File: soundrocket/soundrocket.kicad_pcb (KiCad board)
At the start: 4 copper layers, 85.3 x 45.7 mm, 17 parts, among them J1 XLR3 MALE (OUT), SW1 SW_Push, SW2 RotaryEncoder_Switch, T1 PE-65612NL, U1 Teensy4.0, U2 DIT4192IPW

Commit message: Prototype Revision 2
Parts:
- renumbered R1 to PUR1, R2 to PUR2, R5 to PUR5
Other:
- board text added: "Designed by Daniel A"
- board text added: "sr-proto-rev2"
- board text removed: "Designed by Daniel A."
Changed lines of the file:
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@@
 		(tags "rotary encoder")
 		(property "Reference" "SW2"
-			(at 3 -4.75 0)
+			(at 2.995 -4.866 0)
 			(layer "F.SilkS")
 			(effects
@@
 		(tags "test point THT pad")
 		(property "Reference" "GND"
-			(at 0 -1.648 0)
+			(at 0 -2.032 0)
 			(layer "F.SilkS")
 			(effects
@@
 		)
 		(property "Value" "GND"
-			(at 0 1.75 0)
+			(at 0 2.032 0)
 			(layer "F.Fab")
 			(effects
@@
 		)
 		(fp_text user "GND"
-			(at 0 -1.65 0)
+			(at 0 -2.032 0)
 			(layer "F.Fab")
 			(effects
@@
 		(at 122.428 51.308 -90)
 		(tags "CF14JT10K0 ")
-		(property "Reference" "R5"
-			(at 5.715 0 270)
+		(property "Reference" "PUR5"
+			(at 14.478 0 270)
 			(unlocked yes)
 			(layer "F.SilkS")
@@
 		(tags "test point THT pad")
 		(property "Reference" "5V"
-			(at 0 -1.648 0)
+			(at 0 -2.032 0)
 			(layer "F.SilkS")
 			(effects
@@
 		)
 		(property "Value" "5V"
-			(at 0 1.75 0)
+			(at 0 2.032 0)
 			(layer "F.Fab")
 			(effects
@@
 		)
 		(fp_text user "5V"
-			(at 0 -1.65 0)
+			(at 0 -2.032 0)
 			(layer "F.Fab")
 			(effects
@@
 		(at 165.608 67.31)
 		(tags "CF14JT10K0 ")
-		(property "Reference" "R2"
-			(at 13.462 0 0)
+		(property "Reference" "PUR2"
+			(at 14.478 0 0)
 			(unlocked yes)
 			(layer "F.SilkS")
@@
 		(tags "tact sw push 12mm")
 		(property "Reference" "SW1"
-			(at 5.83 -5.41 90)
+			(at 6.25 9.572 270)
 			(layer "F.SilkS")
 			(effects
@@
 		(at 165.608 71.374)
 		(tags "CF14JT10K0 ")
-		(property "Reference" "R1"
-			(at 13.462 0 0)
+		(property "Reference" "PUR1"
+			(at 14.478 0 0)
 			(unlocked yes)
 			(layer "F.SilkS")
@@
 		)
 	)
-	(gr_text "Designed by Daniel A."
-		(at 130.81 30.226 0)
+	(gr_text "sr-proto-rev2"
+		(at 195.326 71.628 0)
+		(layer "F.SilkS")
+		(effects
+			(font
+				(size 0.8 0.8)
+				(thickness 0.16)
+				(bold yes)
+			)
+			(justify left bottom)
+		)
+	)
+	(gr_text "Designed by Daniel A"
+		(at 191.008 73.152 0)
 		(layer "F.SilkS")
 		(effects
 			(font
-				(size 1.5 1.5)
-				(thickness 0.3)
+				(size 0.8 0.8)
+				(thickness 0.16)
 				(bold yes)
 			)

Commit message: Shrink
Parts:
- removed 5V: 5V, TestPoint:TestPoint_THTPad_D1.5mm_Drill0.7mm
- removed C2, C3, C4: C_Small, KiCad Models:CAPRR254W54L381T254H466
- removed GND: GND, TestPoint:TestPoint_THTPad_D1.5mm_Drill0.7mm
- removed J1: XLR3 MALE (OUT), Connector_Audio:Jack_XLR_Neutrik_NC3MAAV_Vertical
- removed PUR1, PUR2, R3, R4: R_Small (10k), KiCad Models:STA_CF14_STP
- removed PUR5: R_Small, KiCad Models:STA_CF14_STP
- removed SW2: RotaryEncoder_Switch, Rotary_Encoder:RotaryEncoder_Bourns_Vertical_PEC12R-3x17F-Sxxxx
- removed U1: Teensy4.0, KiCad Models:Teensy40
- added REF**: MountingHole_2.2mm_M2, MountingHole:MountingHole_2.2mm_M2, F.Cu at (104.1, 106.7)
- added REF**: MountingHole_2.2mm_M2, MountingHole:MountingHole_2.2mm_M2, F.Cu at (159.0, 116.6)
- added REF**: 2.5mm, TestPoint:TestPoint_THTPad_D2.5mm_Drill1.2mm, F.Cu at (158.4, 110.4)
- added REF**: 2.5mm, TestPoint:TestPoint_THTPad_D2.5mm_Drill1.2mm, F.Cu at (158.4, 106.6)
- added U3: STM32U545CETxQ, KiCad Models:STM32U545CET6Q, F.Cu at (110.2, 112.8)
- moved U2 76.9 mm to (140.6, 110.2), turned to 0 degrees
- moved C1 66.1 mm to (117.6, 116.6), turned to -90 degrees
- moved T1 62.6 mm to (151.6, 111.7), turned to 90 degrees
- moved SW1 40.3 mm to (121.1, 109.0), turned to 0 degrees
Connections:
- U2 pad 11: Net-(U1-21_A7_RX5_BCLK1) -> unconnected-(U2-SCLK-Pad11)
- U2 pad 12: Net-(U1-20_A6_TX5_LRCLK1) -> unconnected-(U2-SYNC-Pad12)
- U2 pad 13: Net-(U1-7_RX2_OUT1A) -> unconnected-(U2-SDATA-Pad13)
- U2 pad 15: Net-(U1-0_RX1_CRX2_CS1) -> unconnected-(U2-RST-Pad15)
- U2 pad 3: Net-(U1-19_A5_SCL0) -> unconnected-(U2-L-Pad3)
- U2 pad 4: Net-(U1-11_MOSI_CTX1) -> unconnected-(U2-CLK1-Pad4)
- U2 pad 5: Net-(U1-10_CS_MQSR) -> unconnected-(U2-CLK0-Pad5)
- U2 pad 6: Net-(U1-23_A9_CRX1_MCLK1) -> unconnected-(U2-MCLK-Pad6)
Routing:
- net 3V3: track 159.1 -> 0.00 mm
- net Net-(U1-0_RX1_CRX2_CS1): track 46.3 -> 0.00 mm, vias 1 -> 0
- net Net-(U1-23_A9_CRX1_MCLK1): track 44.6 -> 0.00 mm, vias 1 -> 0
- net /XLR-TX-: track 40.6 -> 0.00 mm
- net /XLR-TX+: track 39.9 -> 0.00 mm
- net Net-(U1-21_A7_RX5_BCLK1): track 38.0 -> 0.00 mm
- net Net-(U1-6_OUT1D): track 36.9 -> 0.00 mm
- net Net-(U1-7_RX2_OUT1A): track 36.1 -> 0.00 mm, vias 1 -> 0
- net Net-(U1-5_IN2): track 34.5 -> 0.00 mm
- net Net-(U1-19_A5_SCL0): track 34.4 -> 0.00 mm, vias 1 -> 0
- net Net-(U1-20_A6_TX5_LRCLK1): track 33.5 -> 0.00 mm
- net Net-(U1-11_MOSI_CTX1): track 29.4 -> 0.00 mm
- net Net-(U1-10_CS_MQSR): track 27.7 -> 0.00 mm, vias 1 -> 0
- net Net-(C1-Pad1): track 22.5 -> 0.00 mm
- net Net-(U1-3_LRCLK2): track 20.0 -> 0.00 mm
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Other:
- board size 85.3 x 45.7 mm -> 60 x 15 mm
- board text added: "FRONT/TOP"
- board text added: "sr-proto-rev3"
- board text removed: "TX+"
- board text removed: "TX-"
- board text removed: "sr-proto-rev2"

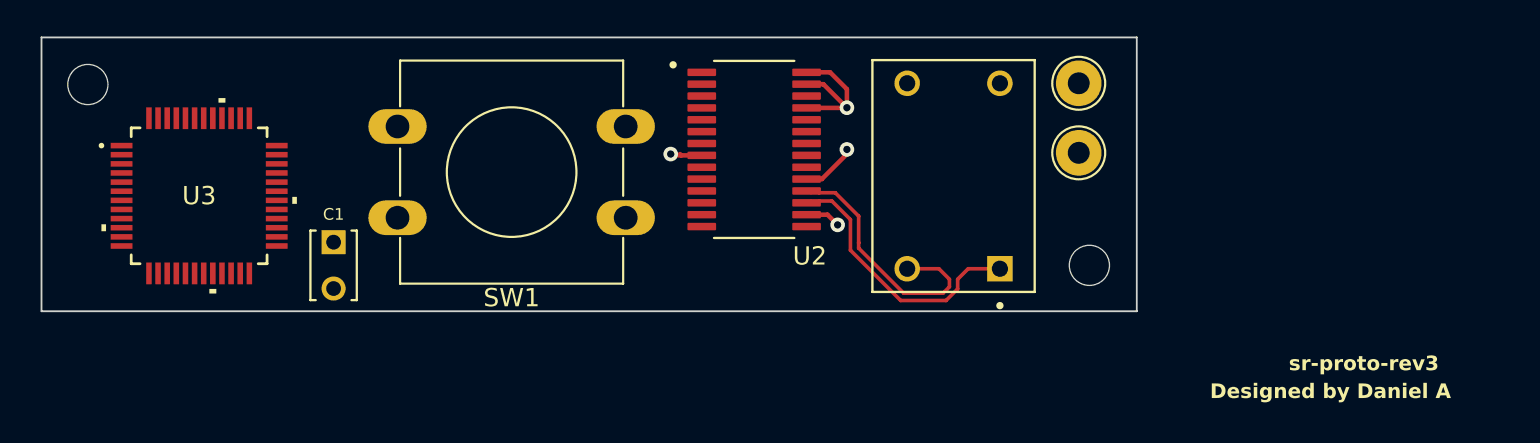
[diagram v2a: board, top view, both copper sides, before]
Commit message: stm32 running out of space
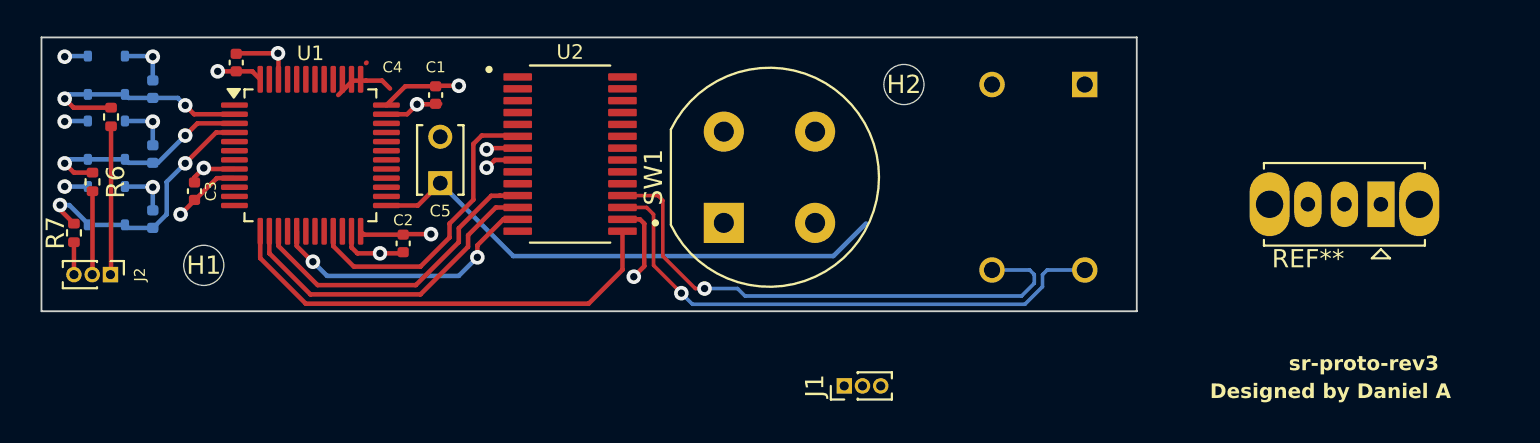
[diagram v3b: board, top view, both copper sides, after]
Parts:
- removed the REF** at (104.1, 106.7)
- removed the REF** at (159.0, 116.6)
- removed the REF** at (158.4, 110.4)
- removed the REF** at (158.4, 106.6)
- removed U3: STM32U545CETxQ, KiCad Models:STM32U545CET6Q
- added C2: C_Small, Capacitor_SMD:C_0402_1005Metric, F.Cu at (121.4, 115.4)
- added C3: C_Small, Capacitor_SMD:C_0402_1005Metric, F.Cu at (110.0, 112.5)
- added C4: C_Small, Capacitor_SMD:C_0402_1005Metric, F.Cu at (112.3, 105.5)
- added C5: C_Small, KiCad Models:CAPRR254W54L381T254H466, F.Cu at (123.4, 110.8)
- added C6: 10nF, Capacitor_SMD:C_0402_1005Metric, B.Cu at (107.7, 106.9)
- added C7: 10nF, Capacitor_SMD:C_0402_1005Metric, B.Cu at (107.7, 110.5)
- added C8: 10nF, Capacitor_SMD:C_0402_1005Metric, B.Cu at (107.7, 114.1)
- added D1: Schottky, Diode_SMD:D_SOD-323, B.Cu at (104.1, 106.2)
- added D2: Schottky, Diode_SMD:D_SOD-323, B.Cu at (106.2, 106.2)
- added D3: Schottky, Diode_SMD:D_SOD-323, B.Cu at (104.1, 109.7)
- added D4: Schottky, Diode_SMD:D_SOD-323, B.Cu at (106.2, 109.7)
- added D5: Schottky, Diode_SMD:D_SOD-323, B.Cu at (104.1, 113.3)
- added D6: Schottky, Diode_SMD:D_SOD-323, B.Cu at (106.2, 113.3)
- added H1: MountingHole, MountingHole:MountingHole_2.2mm_M2, F.Cu at (110.5, 116.6)
- added H2: MountingHole, MountingHole:MountingHole_2.2mm_M2, F.Cu at (148.8, 106.7)
- added J1: XLR_OUT_1x3, Connector_PinHeader_1.00mm:PinHeader_1x03_P1.00mm_Vertical, F.Cu at (145.6, 123.2)
- added J2: XLR_IN_1x3, Connector_PinHeader_1.00mm:PinHeader_1x03_P1.00mm_Vertical, F.Cu at (105.4, 117.1)
- added R5: 200K, Resistor_SMD:R_0402_1005Metric, F.Cu at (105.4, 108.5)
- added R6: 200K, Resistor_SMD:R_0402_1005Metric, F.Cu at (104.4, 112.0)
- added R7: 200K, Resistor_SMD:R_0402_1005Metric, F.Cu at (103.4, 114.8)
- added REF**: SW_Slide_SPDT_Straight_CK_OS102011MS2Q, Button_Switch_THT:SW_Slide_SPDT_Straight_CK_OS102011MS2Q, F.Cu at (175.0, 113.2)
- added U1: STM32F410CBTx, Package_QFP:LQFP-48_7x7mm_P0.5mm, F.Cu at (116.3, 110.6)
- C1: footprint KiCad Models:CAPRR254W54L381T254H466 -> Capacitor_SMD:C_0402_1005Metric
- SW1: footprint Button_Switch_THT:SW_PUSH-12mm -> KiCad Models:SW_D6_C_90
- T1: moved to B.Cu
- moved SW1 20.6 mm to (141.5, 111.8)
- moved C1 10.9 mm to (123.2, 107.3), turned to 90 degrees
- moved U2 10.1 mm to (130.6, 110.5)
- moved T1 4.65 mm to (156.2, 111.8), turned to -90 degrees
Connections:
- net /DIT4192-TX+ renamed TX+
- net /DIT4192-TX- renamed TX-
- C1 pad 1: Net-(C1-Pad1) -> GND
- C1 pad 2: GND -> 3V3
- SW1 pad 2: Net-(C1-Pad1) -> SW1
- U2 pad 11: unconnected-(U2-SCLK-Pad11) -> SCLK
- U2 pad 12: unconnected-(U2-SYNC-Pad12) -> WS
- U2 pad 13: unconnected-(U2-SDATA-Pad13) -> SDATA
- U2 pad 15: unconnected-(U2-RST-Pad15) -> RST
- U2 pad 25: GND -> unconnected-(U2-BLS-Pad25)
- U2 pad 27: GND -> unconnected-(U2-U-Pad27)
- U2 pad 28: GND -> unconnected-(U2-MODE-Pad28)
- U2 pad 6: unconnected-(U2-MCLK-Pad6) -> MCLK
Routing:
- net SW1: track 0.00 -> 29.2 mm
- net RST: track 0.00 -> 25.2 mm
- net 3V3: track 0.00 -> 23.6 mm, vias 0 -> 8
- net WS: track 0.00 -> 18.1 mm
- net SCLK: track 0.00 -> 17.3 mm
- net MCLK: track 0.00 -> 16.6 mm
- net GND: track 12.2 -> 28.2 mm, vias 3 -> 9
- net TX-: track 15.0 -> 30.3 mm, vias 0 -> 1
- net SDATA: track 0.00 -> 15.3 mm, vias 0 -> 2
- net TX+: track 15.0 -> 29.8 mm, vias 0 -> 1
- net IO_XLR_IN3: track 0.00 -> 14.6 mm, vias 0 -> 2
- net IO_XLR_IN1: track 0.00 -> 12.6 mm, vias 0 -> 2
- net IO_XLR_IN2: track 0.00 -> 12.1 mm, vias 0 -> 2
- net XLR_IN1: track 0.00 -> 8.14 mm
- net XLR_IN2: track 0.00 -> 4.58 mm
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- added copper zone on In1.Cu, net 3V3
- removed copper zone on In1.Cu, net 5V0

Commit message: Update soundrocket.kicad_pcb
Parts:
- removed C1: C_Small, Capacitor_SMD:C_0402_1005Metric
- removed C5: C_Small, KiCad Models:CAPRR254W54L381T254H466
- REF**: value SW_Slide_SPDT_Straight_CK_OS102011MS2Q -> Sw_Slide
- moved T1 25.1 mm to (131.1, 112.0)
- moved REF** 24.1 mm to (151.1, 109.5), turned to -90 degrees
- moved H2 10.2 mm to (159.0, 106.7)
- moved J1 5.33 mm to (145.6, 117.9)
- moved U2 2.62 mm to (128.3, 111.8), turned to 90 degrees
- moved SW1 0.98 mm to (140.5, 111.8)
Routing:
- net SW1: track 29.2 -> 0.00 mm
- net TX-: track 30.3 -> 3.68 mm, vias 1 -> 0
- net TX+: track 29.8 -> 3.39 mm, vias 1 -> 0
- net /XLR-TX+: track 0.00 -> 17.8 mm
- net /XLR-TX-: track 0.00 -> 14.6 mm
- net SDATA: track 15.3 -> 21.4 mm
- net MCLK: track 16.6 -> 12.3 mm
- net WS: track 18.1 -> 22.1 mm
- net 3V3: track 23.6 -> 20.6 mm, vias 8 -> 7
- net SCLK: track 17.3 -> 19.7 mm
- net GND: track 28.2 -> 26.7 mm, vias 9 -> 10
- net 5V0: track 0.00 -> 1.39 mm, vias 0 -> 1
- net RST: track 25.2 -> 25.6 mm, vias 0 -> 2
